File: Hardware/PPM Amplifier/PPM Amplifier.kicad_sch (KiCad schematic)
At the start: 16 parts, among them P1 CONN_2, SW1 SW_DIP_x12

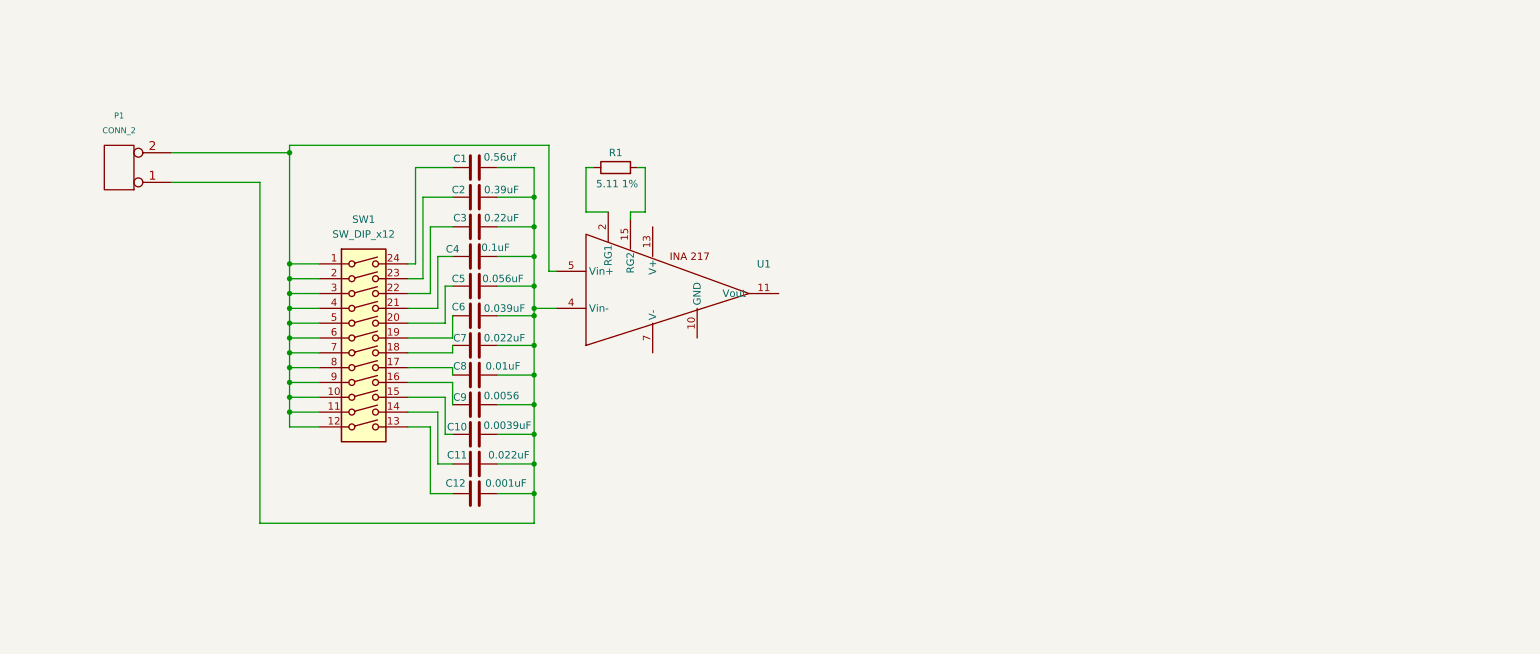
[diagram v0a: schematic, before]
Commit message: PCB for Pulse Controller
First complete schematic for Amplifier
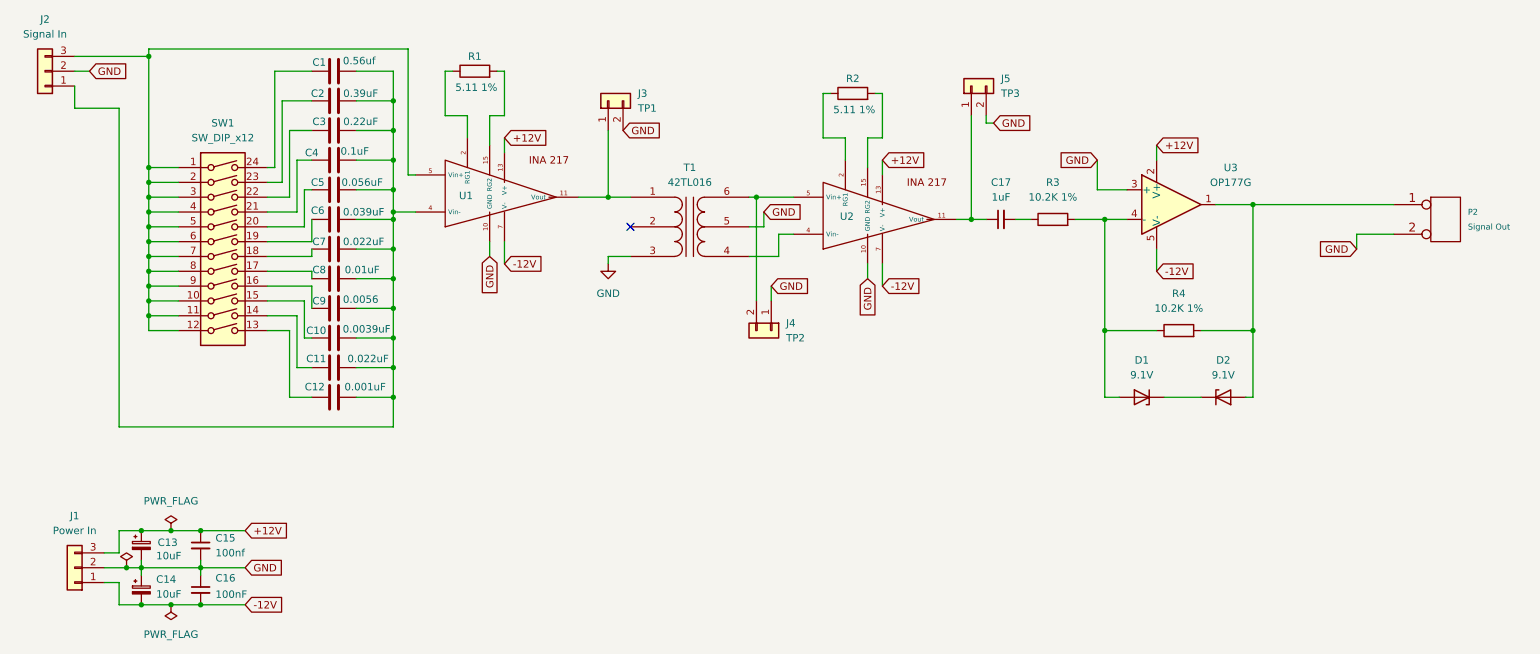
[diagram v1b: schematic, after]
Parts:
- removed P1: CONN_2, symbol DQM:CONN_2
- added C13, C14: 10uF, symbol Device:C_Polarized_Small
- added C15: 100nf, symbol Device:C_Small
- added C16: 100nF, symbol Device:C_Small
- added C17: 1uF, symbol Device:C_Small
- added D1, D2: 9.1V, symbol Device:D_Zener
- added J1: Power In, symbol Connector_Generic:Conn_01x03
- added J2: Signal In, symbol Connector_Generic:Conn_01x03
- added J3: TP1, symbol Connector_Generic:Conn_01x02
- added J4: TP2, symbol Connector_Generic:Conn_01x02
- added J5: TP3, symbol Connector_Generic:Conn_01x02
- added P2: Signal Out, symbol DQM:CONN_2
- added R2: 5.11 1%, symbol Device:R
- added R3, R4: 10.2K 1%, symbol Device:R
- added T1: 42TL016, symbol DQM:Transformer_42TL016
- added U2: ~, symbol DQM:INA217
- added U3: OP177G, Package_TO_SOT_SMD:SOT-23-5, symbol Amplifier_Operational:OP179GRT
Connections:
- net at C1.2, C10.2, C11.2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: now also J2.1 (Pin_1)
- net at SW1.1, SW1.10, SW1.11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: now also J2.3 (Pin_3)
- net GND: now reaches U1.10 (GND)
- net GND: now also C13.2, C14.1, C15.2, C16.1, J1.2 (Pin_2), J2.2 (Pin_2), J3.2 (Pin_2), J4.1 (Pin_1), J5.2 (Pin_2), P2.2 (GND), T1.3 (AB), T1.5 (PB), U2.10 (GND), U3.3 (+)
- net at U1.11 (Vout): now also J3.1 (Pin_1), T1.1 (AA)
- net +12V: now reaches U1.13 (V+)
- net +12V: now also C13.1, C15.1, J1.3 (Pin_3), U2.13 (V+), U3.2 (V+)
- net -12V: now reaches U1.7 (V-)
- net -12V: now also C14.2, C16.2, J1.1 (Pin_1), U2.7 (V-), U3.5 (V-)
- net NC1: no longer names the net of U1.1 (NC1)
- net NC12: no longer names the net of U1.12 (NC12)
- net NC14: no longer names the net of U1.14 (NC14)
- net NC16: no longer names the net of U1.16 (NC16)
- net NC3: no longer names the net of U1.3 (NC3)
- net NC6: no longer names the net of U1.6 (NC6)
- net NC8: no longer names the net of U1.8 (NC8)
- net NC9: no longer names the net of U1.9 (NC9)
- new net: D1.1 (K), D2.1 (K)
- new net: D1.2 (A), R3.2, R4.1, U3.4 (-)
- new net: J4.2 (Pin_2), T1.6 (SB), U2.5 (Vin+)
- new net: C17.1, J5.1 (Pin_1), U2.11 (Vout)
- new net: C17.2, R3.1
- new net: D2.2 (A), P2.1 (VCC), R4.2, U3.1
- new net: R2.1, U2.2 (RG1)
- new net: R2.2, U2.15 (RG2)
- new net: T1.4 (6), U2.4 (Vin-)
- no-connect marks 0 -> 1
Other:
- moved on the sheet: C1, C10, C11, C12, C2, C3, C4, C5, C6, C7, C8, C9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

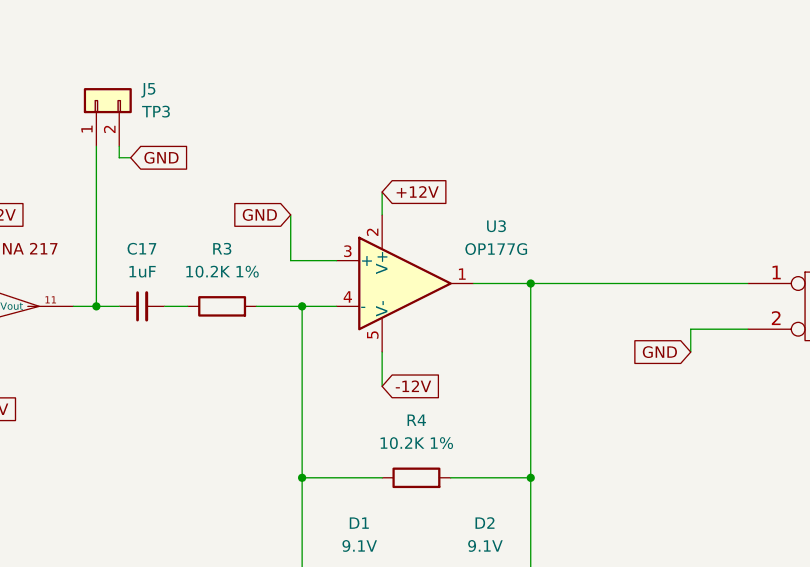
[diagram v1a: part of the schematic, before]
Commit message: PCBS update
Version sent for manufacture for Pulse Controller.
First complete version for Amplipher
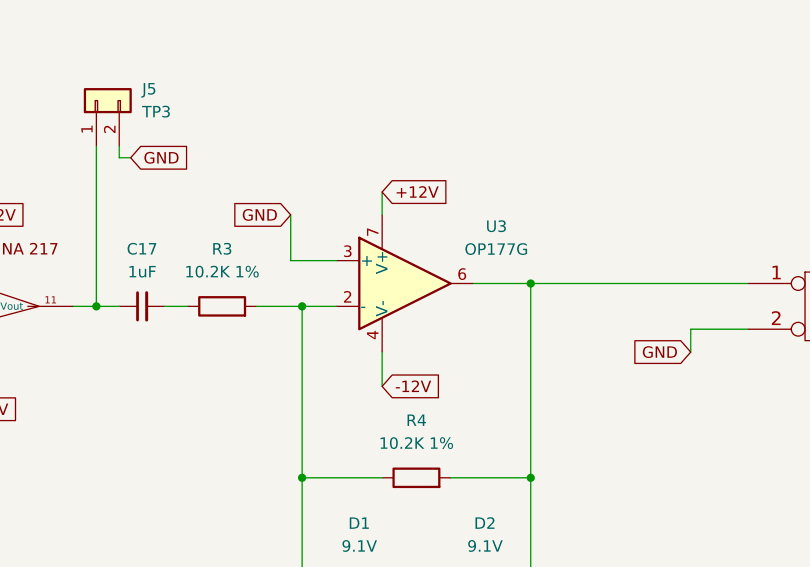
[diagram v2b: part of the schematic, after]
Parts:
- C1, C10, C11, C12, C15, C16, C17, C2, C3, C4, C5, C6, C7, C8, C9: footprint (none) -> Capacitor_SMD:C_0805_2012Metric_Pad1.18x1.45mm_HandSolder
- C13, C14: footprint (none) -> Capacitor_SMD:CP_Elec_5x3
- D1, D2: footprint (none) -> Diode_THT:D_DO-41_SOD81_P7.62mm_Horizontal
- J1, J2: footprint (none) -> Connector_PinHeader_2.54mm:PinHeader_1x03_P2.54mm_Vertical
- J3, J4, J5, P2: footprint (none) -> Connector_PinHeader_2.54mm:PinHeader_1x02_P2.54mm_Vertical
- R1, R2, R3, R4: footprint (none) -> Resistor_SMD:R_0805_2012Metric_Pad1.20x1.40mm_HandSolder
- SW1: footprint (none) -> Button_Switch_THT:SW_DIP_SPSTx12_Slide_6.7x32.04mm_W7.62mm_P2.54mm_LowProfile
- T1: footprint (none) -> DQM_kicad_new:Transformer_42TL016
- U1, U2: footprint (none) -> Package_SO:SOIC-16W_7.5x10.3mm_P1.27mm
- U3: footprint Package_TO_SOT_SMD:SOT-23-5 -> Package_DIP:DIP-8_W7.62mm_LongPads; symbol Amplifier_Operational:OP179GRT -> DQM:OPA177G
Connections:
- net +12V: now also U3.7 (V+); no longer U3.2 (V+)
- net -12V: now also U3.4 (V-); no longer U3.5 (V-)
- net at D1.2 (A), R3.2, R4.1: now also U3.2 (-); no longer U3.4 (-)
- net at D2.2 (A), P2.1 (VCC), R4.2: now also U3.6; no longer U3.1
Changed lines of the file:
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@@
 			)
 		)
-		(property "Footprint" ""
+		(property "Footprint" "Capacitor_SMD:C_0805_2012Metric_Pad1.18x1.45mm_HandSolder"
 			(at 48.26 123.19 0)
 			(effects
@@
 			)
 		)
-		(property "Footprint" ""
+		(property "Footprint" "Diode_THT:D_DO-41_SOD81_P7.62mm_Horizontal"
 			(at 209.55 97.79 0)
 			(effects
@@
 			)
 		)
-		(property "Footprint" ""
+		(property "Footprint" "Connector_PinHeader_2.54mm:PinHeader_1x02_P2.54mm_Vertical"
 			(at 146.05 86.36 0)
 			(effects
@@
 			)
 		)
-		(property "Footprint" ""
+		(property "Footprint" "Capacitor_SMD:C_0805_2012Metric_Pad1.18x1.45mm_HandSolder"
 			(at 74.93 40.9448 0)
 			(effects
@@
 			)
 		)
-		(property "Footprint" ""
+		(property "Footprint" "Capacitor_SMD:C_0805_2012Metric_Pad1.18x1.45mm_HandSolder"
 			(at 74.93 51.1048 0)
 			(effects
@@
 			)
 		)
-		(property "Footprint" ""
+		(property "Footprint" "Capacitor_SMD:C_0805_2012Metric_Pad1.18x1.45mm_HandSolder"
 			(at 185.42 67.31 0)
 			(effects
@@
 			)
 		)
-		(property "Footprint" ""
+		(property "Footprint" "Capacitor_SMD:C_0805_2012Metric_Pad1.18x1.45mm_HandSolder"
 			(at 74.93 61.2648 0)
 			(effects
@@
 			)
 		)
-		(property "Footprint" ""
+		(property "Footprint" "Connector_PinHeader_2.54mm:PinHeader_1x02_P2.54mm_Vertical"
 			(at 261.62 67.31 0)
 			(effects
@@
 					(size 1.524 1.524)
 				)
+				(hide yes)
 			)
 		)
@@
 			)
 		)
-		(property "Footprint" ""
+		(property "Footprint" "Capacitor_SMD:CP_Elec_5x3"
 			(at 38.1 130.81 0)
 			(effects
@@
 			)
 		)
-		(property "Footprint" ""
+		(property "Footprint" "Capacitor_SMD:C_0805_2012Metric_Pad1.18x1.45mm_HandSolder"
 			(at 74.93 96.8248 0)
 			(effects
@@
 			)
 		)
-		(property "Footprint" ""
+		(property "Footprint" "Diode_THT:D_DO-41_SOD81_P7.62mm_Horizontal"
 			(at 223.52 97.79 0)
 			(effects
@@
 			)
 		)
-		(property "Footprint" ""
+		(property "Footprint" "Capacitor_SMD:C_0805_2012Metric_Pad1.18x1.45mm_HandSolder"
 			(at 74.93 81.5848 0)
 			(effects
@@
 			)
 		)
-		(property "Footprint" ""
+		(property "Footprint" "Capacitor_SMD:C_0805_2012Metric_Pad1.18x1.45mm_HandSolder"
 			(at 74.93 86.6648 0)
 			(effects
@@
 			)
 		)
-		(property "Footprint" ""
+		(property "Footprint" "Capacitor_SMD:C_0805_2012Metric_Pad1.18x1.45mm_HandSolder"
 			(at 74.93 71.4248 0)
 			(effects
@@
 			)
 		)
-		(property "Footprint" ""
+		(property "Footprint" "Resistor_SMD:R_0805_2012Metric_Pad1.20x1.40mm_HandSolder"
 			(at 160.02 47.498 90)
 			(effects
@@
 			)
 		)
-		(property "Footprint" ""
+		(property "Footprint" "Resistor_SMD:R_0805_2012Metric_Pad1.20x1.40mm_HandSolder"
 			(at 194.31 69.088 90)
 			(effects
@@
 			)
 		)
-		(property "Footprint" ""
+		(property "Footprint" "Connector_PinHeader_2.54mm:PinHeader_1x03_P2.54mm_Vertical"
 			(at 21.59 41.91 0)
 			(effects
@@
 			)
 		)
-		(property "Footprint" ""
+		(property "Footprint" "Connector_PinHeader_2.54mm:PinHeader_1x02_P2.54mm_Vertical"
 			(at 118.11 46.99 0)
 			(effects
@@
 			)
 		)
-		(property "Footprint" ""
+		(property "Footprint" "Package_SO:SOIC-16W_7.5x10.3mm_P1.27mm"
 			(at 166.37 67.31 0)
 			(effects
@@
 			)
 		)
-		(property "Footprint" ""
+		(property "Footprint" "Resistor_SMD:R_0805_2012Metric_Pad1.20x1.40mm_HandSolder"
 			(at 215.9 88.138 90)
 			(effects
@@
 			)
 		)
-		(property "Footprint" ""
+		(property "Footprint" "Capacitor_SMD:C_0805_2012Metric_Pad1.18x1.45mm_HandSolder"
 			(at 48.26 130.81 0)
 			(effects
@@
 			)
 		)
-		(property "Footprint" ""
+		(property "Footprint" "DQM_kicad_new:Transformer_42TL016"
 			(at 132.08 68.58 0)
 			(effects
@@
 			)
 		)
-		(property "Footprint" ""
+		(property "Footprint" "Capacitor_SMD:C_0805_2012Metric_Pad1.18x1.45mm_HandSolder"
 			(at 74.93 56.1848 0)
 			(effects
@@
 			)
 		)
-		(property "Footprint" ""
+		(property "Footprint" "Capacitor_SMD:C_0805_2012Metric_Pad1.18x1.45mm_HandSolder"
 			(at 74.93 46.0248 0)
 			(effects
@@
 			)
 		)
-		(property "Footprint" ""
+		(property "Footprint" "Capacitor_SMD:C_0805_2012Metric_Pad1.18x1.45mm_HandSolder"
 			(at 74.93 66.3448 0)
 			(effects
@@
 			)
 		)
-		(property "Footprint" ""
+		(property "Footprint" "Capacitor_SMD:C_0805_2012Metric_Pad1.18x1.45mm_HandSolder"
 			(at 74.93 91.7448 0)
 			(effects
@@
 			)
 		)
-		(property "Footprint" ""
+		(property "Footprint" "Button_Switch_THT:SW_DIP_SPSTx12_Slide_6.7x32.04mm_W7.62mm_P2.54mm_LowProfile"
 			(at 52.07 73.66 0)
 			(effects
@@
 			)
 		)
-		(property "Footprint" ""
+		(property "Footprint" "Capacitor_SMD:CP_Elec_5x3"
 			(at 38.1 123.19 0)
 			(effects
@@
 	)
 	(symbol
-		(lib_id "Amplifier_Operational:OP179GRT")
+		(lib_id "DQM:OPA177G")
 		(at 214.63 64.77 0)
 		(unit 1)
@@
 			)
 		)
-		(property "Footprint" "Package_TO_SOT_SMD:SOT-23-5"
+		(property "Footprint" "Package_DIP:DIP-8_W7.62mm_LongPads"
 			(at 214.63 64.77 0)
 			(effects
@@
 		)
 		(property "Datasheet" "https://www.analog.com/media/en/technical-documentation/data-sheets/OP179_279.pdf"
-			(at 214.63 59.69 0)
-			(effects
-				(font
-					(size 1.27 1.27)
-				)
-				(hide yes)
-			)
-		)
-		(property "Description" "Single Rail-to-Rail High Output Current Operational Amplifiers, SOT-23-5"
+			(at 218.44 60.96 0)
+			(effects
+				(font
+					(size 1.27 1.27)
+				)
+				(hide yes)
+			)
+		)
+		(property "Description" "Single Rail-to-Rail High Output Current Operational Amplifiers, SOIC-8"
 			(at 214.63 64.77 0)
 			(effects
@@
 		)
 		(pin "5"
+		)
+		(pin "8"
+		)
+		(pin "7"
+		)
+		(pin "6"
 		)
 		(instances
@@
 			)
 		)
-		(property "Footprint" ""
+		(property "Footprint" "Resistor_SMD:R_0805_2012Metric_Pad1.20x1.40mm_HandSolder"
 			(at 95.25 43.688 90)
 			(effects
@@
 			)
 		)
-		(property "Footprint" ""
+		(property "Footprint" "Connector_PinHeader_2.54mm:PinHeader_1x03_P2.54mm_Vertical"
 			(at 26.67 127 0)
 			(effects
@@
 			)
 		)
-		(property "Footprint" ""
+		(property "Footprint" "Capacitor_SMD:C_0805_2012Metric_Pad1.18x1.45mm_HandSolder"
 			(at 74.93 76.5048 0)
 			(effects
@@
 			)
 		)
-		(property "Footprint" ""
+		(property "Footprint" "Connector_PinHeader_2.54mm:PinHeader_1x02_P2.54mm_Vertical"
 			(at 180.34 44.45 0)
 			(effects
@@
 			)
 		)
-		(property "Footprint" ""
+		(property "Footprint" "Package_SO:SOIC-16W_7.5x10.3mm_P1.27mm"
 			(at 101.6 63.5 0)
 			(effects

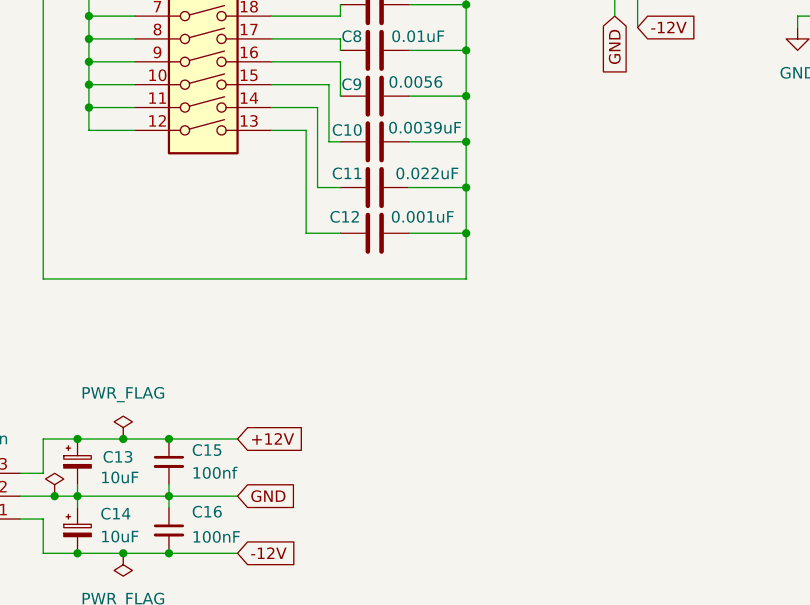
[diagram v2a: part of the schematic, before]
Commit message: Update on Amp Layout
Added power LED
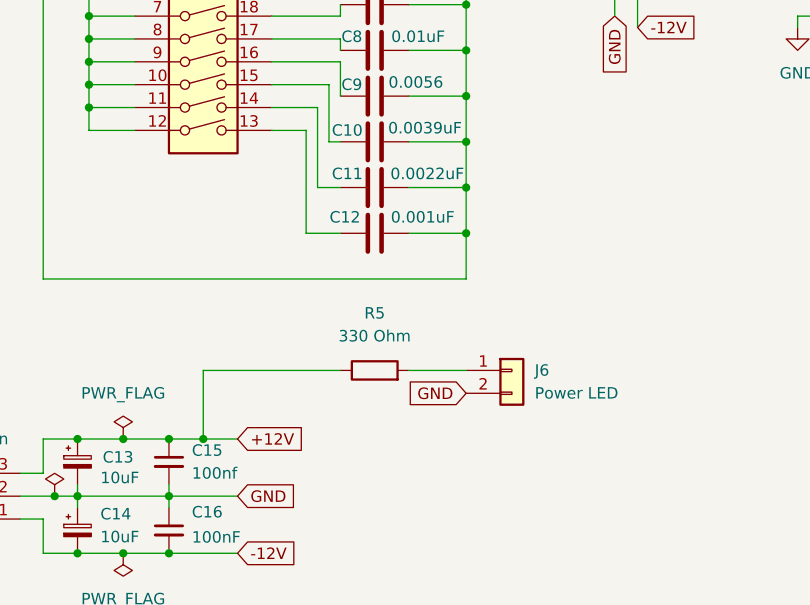
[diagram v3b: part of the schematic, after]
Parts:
- added J6: Power LED, Connector_PinHeader_2.54mm:PinHeader_2x01_P2.54mm_Vertical, symbol Connector_Generic:Conn_01x02
- added R5: 330 Ohm, Resistor_SMD:R_0805_2012Metric_Pad1.20x1.40mm_HandSolder, symbol Device:R
- C11: value 0.022uF -> 0.0022uF
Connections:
- net +12V: now also R5.1
- net GND: now also J6.2 (Pin_2)
- new net: J6.1 (Pin_1), R5.2
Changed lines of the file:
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@@
 	)
 	(junction
+		(at 52.07 120.65)
+		(diameter 0)
+		(color 0 0 0 0)
+	)
+	(junction
 		(at 39.37 39.37)
 		(diameter 0)
@@
 	(wire
 		(pts
+			(xy 74.93 113.03) (xy 81.28 113.03)
+		)
+		(stroke
+			(width 0)
+			(type default)
+		)
+	)
+	(wire
+		(pts
 			(xy 163.83 45.72) (xy 165.1 45.72)
 		)
@@
 	(wire
 		(pts
+			(xy 52.07 113.03) (xy 67.31 113.03)
+		)
+		(stroke
+			(width 0)
+			(type default)
+		)
+	)
+	(wire
+		(pts
 			(xy 74.93 72.39) (xy 81.28 72.39)
 		)
@@
 	(wire
 		(pts
-			(xy 48.26 120.65) (xy 55.88 120.65)
+			(xy 48.26 120.65) (xy 52.07 120.65)
 		)
 		(stroke
@@
 	(wire
 		(pts
+			(xy 52.07 120.65) (xy 52.07 113.03)
+		)
+		(stroke
+			(width 0)
+			(type default)
+		)
+	)
+	(wire
+		(pts
 			(xy 48.26 125.73) (xy 48.26 127)
 		)
@@
 	(wire
 		(pts
+			(xy 52.07 120.65) (xy 55.88 120.65)
+		)
+		(stroke
+			(width 0)
+			(type default)
+		)
+	)
+	(wire
+		(pts
 			(xy 113.03 63.5) (xy 118.11 63.5)
 		)
@@
 	(global_label "GND"
 		(shape input)
+		(at 81.28 115.57 180)
+		(fields_autoplaced yes)
+		(effects
+			(font
+				(size 1.27 1.27)
+			)
+			(justify right)
+		)
+		(property "Intersheetrefs" "${INTERSHEET_REFS}"
+			(at 74.4243 115.57 0)
+			(effects
+				(font
+					(size 1.27 1.27)
+				)
+				(justify right)
+				(hide yes)
+			)
+		)
+	)
+	(global_label "GND"
+		(shape input)
 		(at 144.78 66.04 0)
 		(fields_autoplaced yes)
@@
 	)
 	(symbol
+		(lib_id "Connector_Generic:Conn_01x02")
+		(at 86.36 113.03 0)
+		(unit 1)
+		(exclude_from_sim no)
+		(in_bom yes)
+		(on_board yes)
+		(dnp no)
+		(fields_autoplaced yes)
+		(property "Reference" "J6"
+			(at 88.9 113.0299 0)
+			(effects
+				(font
+					(size 1.27 1.27)
+				)
+				(justify left)
+			)
+		)
+		(property "Value" "Power LED"
+			(at 88.9 115.5699 0)
+			(effects
+				(font
+					(size 1.27 1.27)
+				)
+				(justify left)
+			)
+		)
+		(property "Footprint" "Connector_PinHeader_2.54mm:PinHeader_2x01_P2.54mm_Vertical"
+			(at 86.36 113.03 0)
+			(effects
+				(font
+					(size 1.27 1.27)
+				)
+				(hide yes)
+			)
+		)
+		(property "Datasheet" "~"
+			(at 86.36 113.03 0)
+			(effects
+				(font
+					(size 1.27 1.27)
+				)
+				(hide yes)
+			)
+		)
+		(property "Description" "Generic connector, single row, 01x02, script generated (kicad-library-utils/schlib/autogen/connector/)"
+			(at 86.36 113.03 0)
+			(effects
+				(font
+					(size 1.27 1.27)
+				)
+				(hide yes)
+			)
+		)
+		(pin "2"
+		)
+		(pin "1"
+		)
+		(instances
+			(project ""
+				(path "/71271447-3e13-4e74-82de-a98e46237cb4"
+					(reference "J6")
+					(unit 1)
+				)
+			)
+		)
+	)
+	(symbol
 		(lib_id "Device:C")
 		(at 71.12 92.71 90)
@@
 			)
 		)
-		(property "Value" "0.022uF"
+		(property "Value" "0.0022uF"
 			(at 76.962 91.186 90)
 			(effects
@@
 					(unit 1)
 				)
+			)
+		)
+	)
+	(symbol
+		(lib_id "Device:R")
+		(at 71.12 113.03 90)
+		(unit 1)
+		(exclude_from_sim no)
+		(in_bom yes)
+		(on_board yes)
+		(dnp no)
+		(fields_autoplaced yes)
+		(property "Reference" "R5"
+			(at 71.12 106.68 90)
+			(effects
+				(font
+					(size 1.27 1.27)
+				)
+			)
+		)
+		(property "Value" "330 Ohm"
+			(at 71.12 109.22 90)
+			(effects
+				(font
+					(size 1.27 1.27)
+				)
+			)
+		)
+		(property "Footprint" "Resistor_SMD:R_0805_2012Metric_Pad1.20x1.40mm_HandSolder"
+			(at 71.12 114.808 90)
+			(effects
+				(font
+					(size 1.27 1.27)
+				)
+				(hide yes)
+			)
+		)
+		(property "Datasheet" "~"
+			(at 71.12 113.03 0)
+			(effects
+				(font
+					(size 1.27 1.27)
+				)
+				(hide yes)
+			)
+		)
+		(property "Description" "Resistor"
+			(at 71.12 113.03 0)
+			(effects
+				(font
+					(size 1.27 1.27)
+				)
+				(hide yes)
+			)
+		)
+		(pin "2"
+		)
+		(pin "1"
+		)
+		(instances
+			(project ""
+				(path "/71271447-3e13-4e74-82de-a98e46237cb4"
+					(reference "R5")
+					(unit 1)
+				)

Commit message: Final version of AMP
Sent to manufacture
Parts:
- SW1: footprint Button_Switch_THT:SW_DIP_SPSTx12_Slide_6.7x32.04mm_W7.62mm_P2.54mm_LowProfile -> Button_Switch_SMD:SW_DIP_SPSTx12_Slide_6.7x32.04mm_W8.61mm_P2.54mm_LowProfile
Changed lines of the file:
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@@
 			)
 		)
-		(property "Footprint" "Button_Switch_THT:SW_DIP_SPSTx12_Slide_6.7x32.04mm_W7.62mm_P2.54mm_LowProfile"
+		(property "Footprint" "Button_Switch_SMD:SW_DIP_SPSTx12_Slide_6.7x32.04mm_W8.61mm_P2.54mm_LowProfile"
 			(at 52.07 73.66 0)
 			(effects
